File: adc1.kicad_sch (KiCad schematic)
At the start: 58 parts, among them U5 ADS7953QDBTRQ1

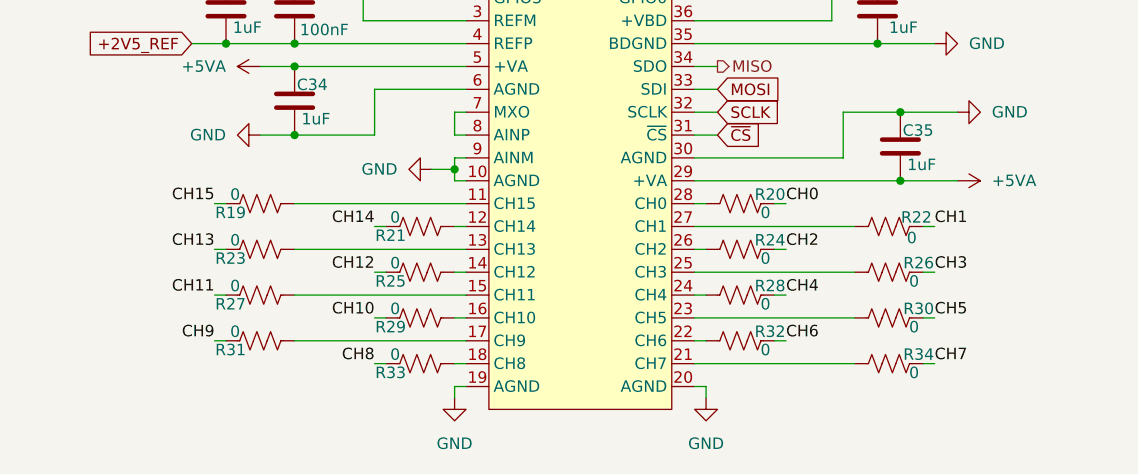
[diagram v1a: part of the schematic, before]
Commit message: remove 0 value resistors
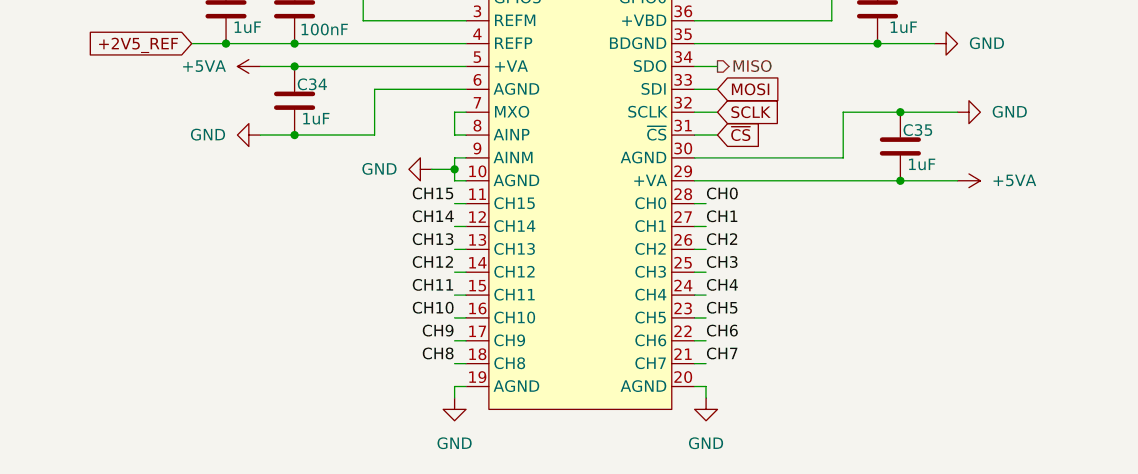
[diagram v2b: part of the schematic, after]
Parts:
- removed R19, R20, R21, R22, R23, R24, R25, R26, R27, R28, R29, R30, R31, R32, R33, R34: 0, Resistor_SMD:R_0603_1608Metric_Pad0.98x0.95mm_HandSolder, symbol Device:R_US
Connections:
- net CH0: now also U5.28 (CH0)
- net CH1: now also U5.27 (CH1)
- net CH10: now also U5.16 (CH10)
- net CH11: now also U5.15 (CH11)
- net CH12: now also U5.14 (CH12)
- net CH13: now also U5.13 (CH13)
- net CH14: now also U5.12 (CH14)
- net CH15: now also U5.11 (CH15)
- net CH2: now also U5.26 (CH2)
- net CH3: now also U5.25 (CH3)
- net CH4: now also U5.24 (CH4)
- net CH5: now also U5.23 (CH5)
- net CH6: now also U5.22 (CH6)
- net CH7: now also U5.21 (CH7)
- net CH8: now also U5.18 (CH8)
- net CH9: now also U5.17 (CH9)

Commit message: PCB layout v1
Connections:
- net MISO renamed ADC_MISO
- net MOSI renamed ADC_MOSI
- net SCLK renamed ADC_SCK

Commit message: progress towards v2
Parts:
- added R34: 33, Resistor_SMD:R_0402_1005Metric, symbol Device:R_US
- R15, R16, R17, R18: footprint Resistor_SMD:R_0603_1608Metric_Pad0.98x0.95mm_HandSolder -> Resistor_SMD:R_0402_1005Metric
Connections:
- net ADC_MISO: no longer names the net of U5.34 (SDO)
- net ADC_MISO: now also R34.1
- net ADC_MOSI renamed MOSI
- net ADC_SCK renamed SCLK
- net ~{CS} renamed CS_N
- new net MISO: R34.2
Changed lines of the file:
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@@
 	(wire
 		(pts
-			(xy 132.08 127) (xy 134.62 127)
+			(xy 132.08 127) (xy 146.05 127)
 		)
 		(stroke
@@
 	(wire
 		(pts
+			(xy 153.67 127) (xy 156.21 127)
+		)
+		(stroke
+			(width 0)
+			(type default)
+		)
+	)
+	(wire
+		(pts
 			(xy 19.05 36.83) (xy 24.13 36.83)
 		)
@@
 		)
 	)
-	(global_label "ADC_MOSI"
+	(global_label "+2V5_REF"
 		(shape input)
-		(at 134.62 129.54 0)
+		(at 76.2 124.46 180)
 		(fields_autoplaced yes)
 		(effects
@@
 				(size 1.27 1.27)
 			)
-			(justify left)
+			(justify right)
 		)
 		(property "Intersheetrefs" "${INTERSHEET_REFS}"
-			(at 146.7976 129.54 0)
+			(at 63.6596 124.46 0)
 			(hide yes)
 			(show_name no)
@@
 					(size 1.27 1.27)
 				)
-				(justify left)
+				(justify right)
 			)
 		)
 	)
-	(global_label "ADC_MISO"
-		(shape input)
-		(at 134.62 127 0)
-		(fields_autoplaced yes)
+	(hierarchical_label "MISO"
+		(shape output)
+		(at 156.21 127 0)
 		(effects
 			(font
@@
 			(justify left)
 		)
-		(property "Intersheetrefs" "${INTERSHEET_REFS}"
-			(at 146.7976 127 0)
-			(hide yes)
-			(show_name no)
-			(do_not_autoplace no)
-			(effects
-				(font
-					(size 1.27 1.27)
-				)
-				(justify left)
-			)
-		)
 	)
-	(global_label "ADC_SCK"
-		(shape input)
-		(at 134.62 132.08 0)
-		(fields_autoplaced yes)
+	(hierarchical_label "CS_N"
+		(shape output)
+		(at 134.62 134.62 0)
 		(effects
 			(font
@@
 			(justify left)
 		)
-		(property "Intersheetrefs" "${INTERSHEET_REFS}"
-			(at 145.9509 132.08 0)
-			(hide yes)
-			(show_name no)
-			(do_not_autoplace no)
-			(effects
-				(font
-					(size 1.27 1.27)
-				)
-				(justify left)
-			)
-		)
 	)
-	(global_label "+2V5_REF"
-		(shape input)
-		(at 76.2 124.46 180)
-		(fields_autoplaced yes)
+	(hierarchical_label "MOSI"
+		(shape output)
+		(at 134.62 129.54 0)
 		(effects
 			(font
 				(size 1.27 1.27)
 			)
-			(justify right)
-		)
-		(property "Intersheetrefs" "${INTERSHEET_REFS}"
-			(at 63.6596 124.46 0)
-			(hide yes)
-			(show_name no)
-			(do_not_autoplace no)
-			(effects
-				(font
-					(size 1.27 1.27)
-				)
-				(justify right)
-			)
+			(justify left)
 		)
 	)
-	(hierarchical_label "~{CS}"
-		(shape input)
-		(at 134.62 134.62 0)
+	(hierarchical_label "SCLK"
+		(shape output)
+		(at 134.62 132.08 0)
 		(effects
 			(font
@@
 			)
 		)
-		(property "Footprint" "Resistor_SMD:R_0603_1608Metric_Pad0.98x0.95mm_HandSolder"
+		(property "Footprint" "Resistor_SMD:R_0402_1005Metric"
 			(at 134.874 111.506 90)
 			(hide yes)
@@
 	(symbol
 		(lib_id "Device:R_US")
+		(at 149.86 127 90)
+		(unit 1)
+		(body_style 1)
+		(exclude_from_sim no)
+		(in_bom yes)
+		(on_board yes)
+		(in_pos_files yes)
+		(dnp no)
+		(property "Reference" "R34"
+			(at 145.542 125.984 90)
+			(show_name no)
+			(do_not_autoplace no)
+			(effects
+				(font
+					(size 1.27 1.27)
+				)
+			)
+		)
+		(property "Value" "33"
+			(at 152.908 125.984 90)
+			(show_name no)
+			(do_not_autoplace no)
+			(effects
+				(font
+					(size 1.27 1.27)
+				)
+			)
+		)
+		(property "Footprint" "Resistor_SMD:R_0402_1005Metric"
+			(at 150.114 125.984 90)
+			(hide yes)
+			(show_name no)
+			(do_not_autoplace no)
+			(effects
+				(font
+					(size 1.27 1.27)
+				)
+			)
+		)
+		(property "Datasheet" ""
+			(at 149.86 127 0)
+			(hide yes)
+			(show_name no)
+			(do_not_autoplace no)
+			(effects
+				(font
+					(size 1.27 1.27)
+				)
+			)
+		)
+		(property "Description" "Resistor, US symbol"
+			(at 149.86 127 0)
+			(hide yes)
+			(show_name no)
+			(do_not_autoplace no)
+			(effects
+				(font
+					(size 1.27 1.27)
+				)
+			)
+		)
+		(property "LCSC Part" "C23140"
+			(at 149.86 127 90)
+			(hide yes)
+			(show_name no)
+			(do_not_autoplace no)
+			(effects
+				(font
+					(size 1.27 1.27)
+				)
+			)
+		)
+		(pin "2"
+		)
+		(pin "1"
+		)
+		(instances
+			(project "stav-keeb-65"
+				(path "/f067c205-942c-45af-b694-038ca43c147c/102b9583-fe1e-454e-b472-c731d3a32681"
+					(reference "R37")
+					(unit 1)
+				)
+				(path "/f067c205-942c-45af-b694-038ca43c147c/7ed9120e-f11c-4b22-935f-1ee89d31afd6"
+					(reference "R34")
+					(unit 1)
+				)
+				(path "/f067c205-942c-45af-b694-038ca43c147c/a1b97858-44bd-4201-b050-5e153f225d6a"
+					(reference "R36")
+					(unit 1)
+				)
+				(path "/f067c205-942c-45af-b694-038ca43c147c/c1663012-812f-4121-9717-99888f6b08f2"
+					(reference "R35")
+					(unit 1)
+				)
+			)
+		)
+	)
+	(symbol
+		(lib_id "Device:R_US")
 		(at 105.41 111.76 180)
 		(unit 1)
@@
 			)
 		)
-		(property "Footprint" "Resistor_SMD:R_0603_1608Metric_Pad0.98x0.95mm_HandSolder"
+		(property "Footprint" "Resistor_SMD:R_0402_1005Metric"
 			(at 104.394 111.506 90)
 			(hide yes)
@@
 			)
 		)
-		(property "Footprint" "Resistor_SMD:R_0603_1608Metric_Pad0.98x0.95mm_HandSolder"
+		(property "Footprint" "Resistor_SMD:R_0402_1005Metric"
 			(at 141.224 111.506 90)
 			(hide yes)
@@
 			)
 		)
-		(property "Footprint" "Resistor_SMD:R_0603_1608Metric_Pad0.98x0.95mm_HandSolder"
+		(property "Footprint" "Resistor_SMD:R_0402_1005Metric"
 			(at 98.044 111.506 90)
 			(hide yes)

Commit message: more progress towards v2
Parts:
- C31, C32, C33, C34, C35, K_C1, K_C10, K_C11, K_C12, K_C13, K_C14, K_C15, K_C16, K_C2, K_C3, K_C4, K_C5, K_C6, K_C7, K_C8, K_C9: footprint Capacitor_SMD:C_0603_1608Metric_Pad1.08x0.95mm_HandSolder -> Capacitor_SMD:C_0402_1005Metric
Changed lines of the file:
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@@
 			)
 		)
-		(property "Footprint" "Capacitor_SMD:C_0603_1608Metric_Pad1.08x0.95mm_HandSolder"
+		(property "Footprint" "Capacitor_SMD:C_0402_1005Metric"
 			(at 80.9752 124.46 0)
 			(hide yes)
@@
 			)
 		)
-		(property "Footprint" "Capacitor_SMD:C_0603_1608Metric_Pad1.08x0.95mm_HandSolder"
+		(property "Footprint" "Capacitor_SMD:C_0402_1005Metric"
 			(at 75.2348 73.66 0)
 			(hide yes)
@@
 			)
 		)
-		(property "Footprint" "Capacitor_SMD:C_0603_1608Metric_Pad1.08x0.95mm_HandSolder"
+		(property "Footprint" "Capacitor_SMD:C_0402_1005Metric"
 			(at 49.8348 38.1 0)
 			(hide yes)
@@
 			)
 		)
-		(property "Footprint" "Capacitor_SMD:C_0603_1608Metric_Pad1.08x0.95mm_HandSolder"
+		(property "Footprint" "Capacitor_SMD:C_0402_1005Metric"
 			(at 207.3148 38.1 0)
 			(hide yes)
@@
 			)
 		)
-		(property "Footprint" "Capacitor_SMD:C_0603_1608Metric_Pad1.08x0.95mm_HandSolder"
+		(property "Footprint" "Capacitor_SMD:C_0402_1005Metric"
 			(at 86.6648 116.84 0)
 			(hide yes)
@@
 			)
 		)
-		(property "Footprint" "Capacitor_SMD:C_0603_1608Metric_Pad1.08x0.95mm_HandSolder"
+		(property "Footprint" "Capacitor_SMD:C_0402_1005Metric"
 			(at 155.9052 139.7 0)
 			(hide yes)
@@
 			)
 		)
-		(property "Footprint" "Capacitor_SMD:C_0603_1608Metric_Pad1.08x0.95mm_HandSolder"
+		(property "Footprint" "Capacitor_SMD:C_0402_1005Metric"
 			(at 75.2348 38.1 0)
 			(hide yes)
@@
 			)
 		)
-		(property "Footprint" "Capacitor_SMD:C_0603_1608Metric_Pad1.08x0.95mm_HandSolder"
+		(property "Footprint" "Capacitor_SMD:C_0402_1005Metric"
 			(at 101.9048 73.66 0)
 			(hide yes)
@@
 			)
 		)
-		(property "Footprint" "Capacitor_SMD:C_0603_1608Metric_Pad1.08x0.95mm_HandSolder"
+		(property "Footprint" "Capacitor_SMD:C_0402_1005Metric"
 			(at 23.1648 73.66 0)
 			(hide yes)
@@
 			)
 		)
-		(property "Footprint" "Capacitor_SMD:C_0603_1608Metric_Pad1.08x0.95mm_HandSolder"
+		(property "Footprint" "Capacitor_SMD:C_0402_1005Metric"
 			(at 155.2448 73.66 0)
 			(hide yes)
@@
 			)
 		)
-		(property "Footprint" "Capacitor_SMD:C_0603_1608Metric_Pad1.08x0.95mm_HandSolder"
+		(property "Footprint" "Capacitor_SMD:C_0402_1005Metric"
 			(at 88.5952 134.62 0)
 			(hide yes)
@@
 			)
 		)
-		(property "Footprint" "Capacitor_SMD:C_0603_1608Metric_Pad1.08x0.95mm_HandSolder"
+		(property "Footprint" "Capacitor_SMD:C_0402_1005Metric"
 			(at 153.3652 124.46 0)
 			(hide yes)
@@
 			)
 		)
-		(property "Footprint" "Capacitor_SMD:C_0603_1608Metric_Pad1.08x0.95mm_HandSolder"
+		(property "Footprint" "Capacitor_SMD:C_0402_1005Metric"
 			(at 49.8348 73.66 0)
 			(hide yes)
@@
 			)
 		)
-		(property "Footprint" "Capacitor_SMD:C_0603_1608Metric_Pad1.08x0.95mm_HandSolder"
+		(property "Footprint" "Capacitor_SMD:C_0402_1005Metric"
 			(at 155.2448 38.1 0)
 			(hide yes)
@@
 			)
 		)
-		(property "Footprint" "Capacitor_SMD:C_0603_1608Metric_Pad1.08x0.95mm_HandSolder"
+		(property "Footprint" "Capacitor_SMD:C_0402_1005Metric"
 			(at 128.5748 73.66 0)
 			(hide yes)
@@
 			)
 		)
-		(property "Footprint" "Capacitor_SMD:C_0603_1608Metric_Pad1.08x0.95mm_HandSolder"
+		(property "Footprint" "Capacitor_SMD:C_0402_1005Metric"
 			(at 180.6448 73.66 0)
 			(hide yes)
@@
 			)
 		)
-		(property "Footprint" "Capacitor_SMD:C_0603_1608Metric_Pad1.08x0.95mm_HandSolder"
+		(property "Footprint" "Capacitor_SMD:C_0402_1005Metric"
 			(at 23.1648 38.1 0)
 			(hide yes)
@@
 			)
 		)
-		(property "Footprint" "Capacitor_SMD:C_0603_1608Metric_Pad1.08x0.95mm_HandSolder"
+		(property "Footprint" "Capacitor_SMD:C_0402_1005Metric"
 			(at 128.5748 38.1 0)
 			(hide yes)
@@
 			)
 		)
-		(property "Footprint" "Capacitor_SMD:C_0603_1608Metric_Pad1.08x0.95mm_HandSolder"
+		(property "Footprint" "Capacitor_SMD:C_0402_1005Metric"
 			(at 180.6448 38.1 0)
 			(hide yes)
@@
 			)
 		)
-		(property "Footprint" "Capacitor_SMD:C_0603_1608Metric_Pad1.08x0.95mm_HandSolder"
+		(property "Footprint" "Capacitor_SMD:C_0402_1005Metric"
 			(at 207.3148 73.66 0)
 			(hide yes)
@@
 			)
 		)
-		(property "Footprint" "Capacitor_SMD:C_0603_1608Metric_Pad1.08x0.95mm_HandSolder"
+		(property "Footprint" "Capacitor_SMD:C_0402_1005Metric"
 			(at 101.9048 38.1 0)
 			(hide yes)
